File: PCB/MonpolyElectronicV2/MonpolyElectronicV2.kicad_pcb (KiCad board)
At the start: 2 copper layers, 0.7 x 0.5 mm, 92 parts, among them J1 Conn_01x14, J2 10155435-00011LF, J3 2171820001, J4 Conn_01x05, J5 Conn_01x04, J6 Conn_01x10, J7 Conn_01x05, Q1 NPN, Q2 NPN, Q3 AO3400A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

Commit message: finish placement of all components
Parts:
- added J10: Conn_01x01, Connector_PinHeader_2.54mm:PinHeader_1x01_P2.54mm_Vertical, F.Cu at (-47.0, 71.7)
- added J11: Conn_01x01, Connector_PinHeader_2.54mm:PinHeader_1x01_P2.54mm_Vertical, F.Cu at (-36.6, 86.0)
- added J12: Conn_01x01, Connector_PinHeader_2.54mm:PinHeader_1x01_P2.54mm_Vertical, F.Cu at (-20.2, 74.2)
- added J13: Conn_01x01, Connector_PinHeader_2.54mm:PinHeader_1x01_P2.54mm_Vertical, F.Cu at (-13.2, 73.0)
- added J14: Conn_01x01, Connector_PinHeader_2.54mm:PinHeader_1x01_P2.54mm_Vertical, F.Cu at (-16.7, 71.7)
- added J15: Conn_01x01, Connector_PinHeader_2.54mm:PinHeader_1x01_P2.54mm_Vertical, F.Cu at (-20.2, 70.5)
- added J16: Conn_01x01, Connector_PinHeader_2.54mm:PinHeader_1x01_P2.54mm_Vertical, F.Cu at (-26.5, 89.5)
- added J17: Conn_01x01, Connector_PinHeader_2.54mm:PinHeader_1x01_P2.54mm_Vertical, F.Cu at (-39.2, 89.5)
- added J18: Conn_01x01, Connector_PinHeader_2.54mm:PinHeader_1x01_P2.54mm_Vertical, F.Cu at (-29.1, 86.0)
- added J19: Conn_01x01, Connector_PinHeader_2.54mm:PinHeader_1x01_P2.54mm_Vertical, F.Cu at (-27.8, 93.0)
- added J8: Conn_01x01, Connector_PinHeader_2.54mm:PinHeader_1x01_P2.54mm_Vertical, F.Cu at (-20.2, 66.6)
- added J9: Conn_01x01, Connector_PinHeader_2.54mm:PinHeader_1x01_P2.54mm_Vertical, F.Cu at (-40.5, 86.0)
- added JP7: SolderJumper_2_Open, Jumper:SolderJumper-2_P1.3mm_Open_TrianglePad1.0x1.5mm, F.Cu at (176.4, 77.2)
- added R26: 10k, Resistor_SMD:R_0603_1608Metric, F.Cu at (-21.9, 80.5)
- C18: value 0.1uF -> 10uF
- J6: value Conn_01x10 -> Conn_01x01; footprint Connector_PinHeader_2.54mm:PinHeader_1x10_P2.54mm_Vertical -> Connector_PinHeader_2.54mm:PinHeader_1x01_P2.54mm_Vertical
- J7: value Conn_01x05 -> Conn_01x01; footprint Connector_PinHeader_2.54mm:PinHeader_1x05_P2.54mm_Vertical -> Connector_PinHeader_2.54mm:PinHeader_1x01_P2.54mm_Vertical
- R13: value 10k -> 100
- SW1, SW2, SW3: footprint Button_Switch_THT:SW_PUSH-12mm -> Extra:SW_TL1105BF160Q
- moved R14 146.3 mm to (-45.1, 67.2), turned to 180 degrees
- moved J5 142.7 mm to (129.8, 161.8), turned to -90 degrees
- moved C18 141.5 mm to (-44.2, 64.8), turned to 90 degrees
- moved JP4 136.3 mm to (182.8, 74.6), turned to 180 degrees
- moved JP5 133.9 mm to (182.8, 80.6), turned to 180 degrees
- moved R21 131.5 mm to (175.5, 70.6), turned to 90 degrees
- moved JP6 130.7 mm to (182.8, 87.4), turned to 180 degrees
- moved Q3 127.4 mm to (177.9, 81.5), turned to 90 degrees
- moved JP1 124.9 mm to (170.8, 74.6), turned to 180 degrees
- moved Q4 124.3 mm to (178.3, 89.1), turned to 90 degrees
- moved R23 122.6 mm to (177.9, 84.4)
- moved JP2 122.4 mm to (170.8, 80.6), turned to 180 degrees
- moved R22 120.4 mm to (174.5, 84.4)
- moved R25 119.9 mm to (178.3, 92.0), turned to 180 degrees
- moved JP3 119.2 mm to (170.8, 87.4), turned to 180 degrees
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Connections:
- C18 pad 1: GND -> +3.3V
- C18 pad 2: IO0 -> GND
- C19 pad 1: GND -> EN
- C19 pad 2: EN -> GND
- JP4 pad 2: Net-(JP1-A) -> Net-(JP4-B)
- R13 pad 1: IO0 -> Net-(JP1-A)
- R13 pad 2: +3.3V -> Net-(JP4-B)
- U1 pad 15: Net-(J7-Pin_3) -> Net-(J9-Pin_1)
- U1 pad 16: Net-(J6-Pin_7) -> Net-(J17-Pin_1)
- U1 pad 18: Net-(J7-Pin_5) -> Net-(J11-Pin_1)
- U1 pad 24: Net-(J6-Pin_8) -> Net-(J18-Pin_1)
- U1 pad 25: Net-(J6-Pin_9) -> Net-(J19-Pin_1)
- U1 pad 26: Net-(J6-Pin_6) -> Net-(J16-Pin_1)
- U1 pad 32: Net-(J6-Pin_2) -> Net-(J12-Pin_1)
- U1 pad 33: Net-(J6-Pin_3) -> Net-(J13-Pin_1)
- U1 pad 34: Net-(J6-Pin_4) -> Net-(J14-Pin_1)
- U1 pad 35: Net-(J6-Pin_5) -> Net-(J15-Pin_1)
- U1 pad 38: Net-(J7-Pin_2) -> Net-(J8-Pin_1)
- U1 pad 7: Net-(J7-Pin_4) -> Net-(J10-Pin_1)
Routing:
- net ESP32_D+: track 0.00 -> 6.09 mm
- net ESP32_D-: track 0.00 -> 6.04 mm
- net D-: track 2.62 -> 0.00 mm
- net D+: track 2.62 -> 0.00 mm

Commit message: finish placing components
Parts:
- BT1, TH1: moved to B.Cu
- J1: footprint Connector_PinHeader_2.54mm:PinHeader_1x14_P2.54mm_Vertical -> Extra:240X320 TFT 3.2 display
- moved C17 232.7 mm to (182.4, 102.3), turned to 0 degrees
- moved R5 232.0 mm to (171.2, 102.9), turned to -90 degrees
- moved C20 231.4 mm to (182.4, 103.8), turned to 0 degrees
- moved C18 230.3 mm to (182.4, 105.2), turned to 0 degrees
- moved R6 230.2 mm to (169.6, 102.9), turned to -90 degrees
- moved R14 228.2 mm to (180.0, 104.4), turned to 90 degrees
- moved J10 224.6 mm to (175.5, 102.5), turned to -90 degrees
- moved U1 216.4 mm to (177.8, 116.0), turned to -90 degrees
- moved R18 212.7 mm to (165.5, 102.8)
- moved R19 212.7 mm to (165.5, 104.4)
- moved J8 210.4 mm to (180.6, 129.2), turned to -90 degrees
- moved J7 209.7 mm to (181.8, 132.8), turned to -90 degrees
- moved J15 205.6 mm to (176.7, 129.2), turned to -90 degrees
- moved J9 203.1 mm to (161.2, 109.0), turned to -90 degrees
- moved J14 201.7 mm to (175.5, 132.8), turned to -90 degrees
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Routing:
- net D-: track 0.00 -> 30.2 mm, vias 0 -> 2
- net D+: track 0.00 -> 27.7 mm, vias 0 -> 2
- net ESP32_D-: track 6.04 -> 18.3 mm
- net ESP32_D+: track 6.09 -> 18.0 mm
- net /Logic/SCL: track 0.00 -> 10.5 mm, vias 0 -> 2
- net VUSB: track 0.00 -> 5.22 mm
- net Net-(U1-USB_D-): track 0.00 -> 5.14 mm
- net /Logic/SDA: track 0.00 -> 4.40 mm
- net Net-(U1-USB_D+): track 0.00 -> 2.86 mm
- net GND: track 0.00 -> 0.93 mm, vias 0 -> 1
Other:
- board size 0.7 x 0.5 mm -> 93.3 x 128.4 mm
- board text added: "NFC Module"

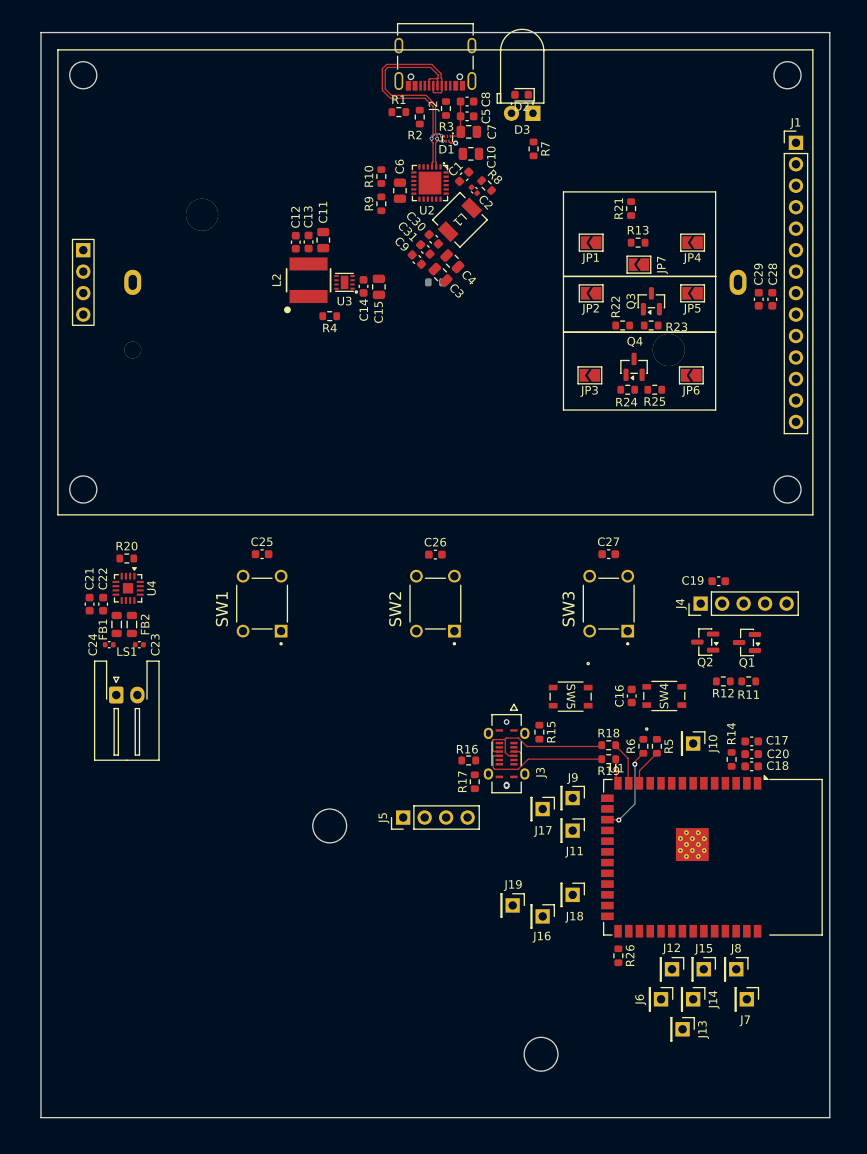
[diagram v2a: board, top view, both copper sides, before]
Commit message: start routing top part of the pcb
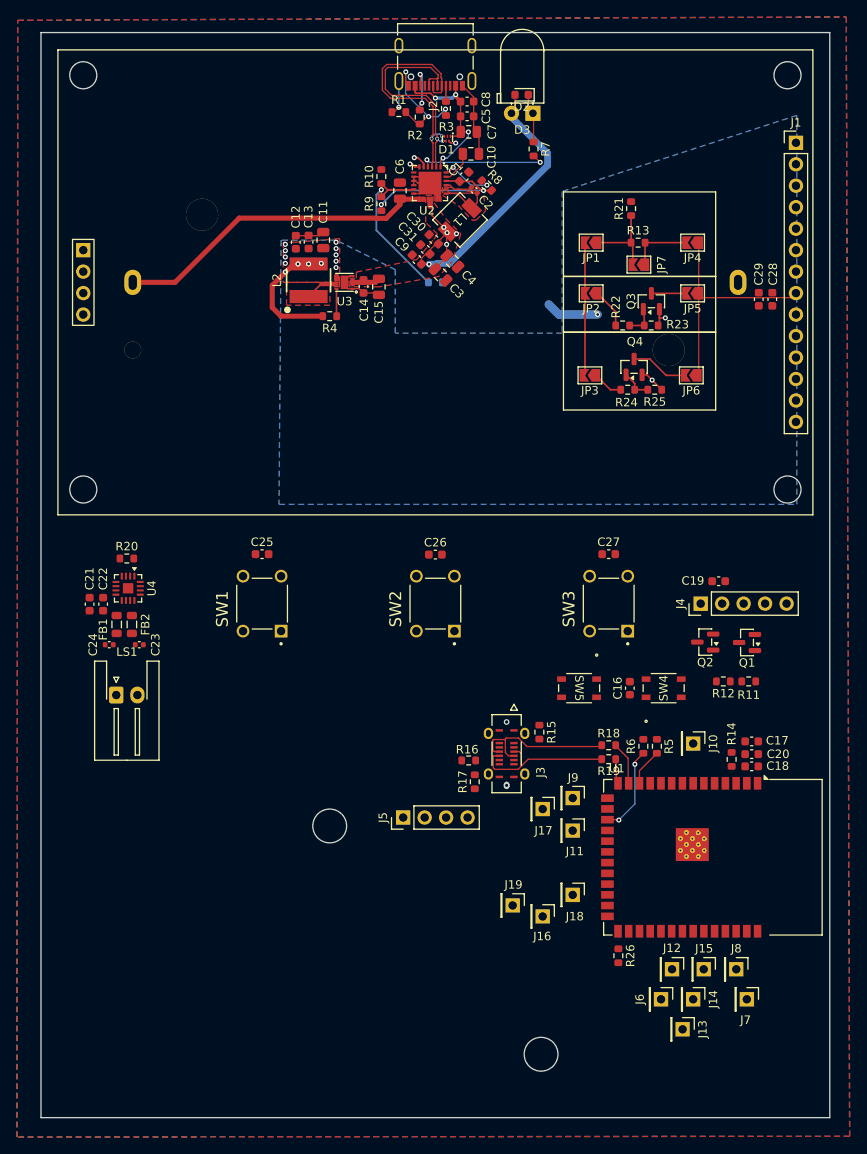
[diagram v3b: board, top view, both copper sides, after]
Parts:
- moved SW5 1.41 mm to (162.0, 96.0)
- moved C16 0.95 mm to (168.0, 96.0)
- moved SW4 0.93 mm to (172.0, 96.0)
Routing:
- net GND: track 0.93 -> 54.2 mm, vias 1 -> 6
- net SYS: track 0.00 -> 51.3 mm, vias 0 -> 5
- net BAT: track 0.00 -> 39.0 mm
- net TFT_LED: track 0.00 -> 27.7 mm
- net TS: track 0.00 -> 23.6 mm, vias 0 -> 1
- net REGN: track 0.00 -> 19.4 mm, vias 0 -> 2
- net +3.3V: track 0.00 -> 17.8 mm, vias 0 -> 14
- net Net-(JP1-B): track 0.00 -> 15.8 mm
- net Net-(U2-STAT): track 0.00 -> 15.5 mm, vias 0 -> 2
- net VUSB: track 5.22 -> 20.0 mm, vias 0 -> 4
- net Net-(JP1-A): track 0.00 -> 9.88 mm
- net Net-(C2-Pad2): track 0.00 -> 9.63 mm
- net Net-(JP4-B): track 0.00 -> 7.50 mm
- net Net-(JP6-B): track 0.00 -> 6.85 mm
- net DSEL: track 0.00 -> 6.79 mm, vias 0 -> 2
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- added copper zone on B.Cu, net +3.3V
- added copper zone on F.Cu, net +3.3V
- added copper zone on B.Cu, net GND
- added copper zone on F.Cu, net GND
- added copper zone on F.Cu, net Net-(C2-Pad2)
- added copper zone on F.Cu, net Net-(U3-SW)
- added copper zone on F.Cu, net SYS

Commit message: Finish routing PCB
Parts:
- removed J11, J17, J6, J9: Conn_01x01, Connector_PinHeader_2.54mm:PinHeader_1x01_P2.54mm_Vertical
- moved C27 41.0 mm to (124.5, 80.2)
- moved C25 41.0 mm to (165.4, 80.1)
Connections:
- U1 pad 15: Net-(J9-Pin_1) -> SW1
- U1 pad 16: Net-(J17-Pin_1) -> SW3
- U1 pad 18: Net-(J11-Pin_1) -> SW2
- U1 pad 31: Net-(J6-Pin_1) -> TFT_RESET
- U1 pad 8: TFT_RESET -> unconnected-(U1-IO15-Pad8)
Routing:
- net +3.3V: track 17.8 -> 240.1 mm, vias 14 -> 21
- net /Logic/SCL: track 12.3 -> 128.8 mm, vias 3 -> 6
- net /Logic/SDA: track 5.65 -> 122.1 mm, vias 1 -> 4
- net TFT_CS: track 0.00 -> 103.0 mm, vias 0 -> 2
- net Net-(JP1-B): track 15.8 -> 110.0 mm, vias 0 -> 2
- net TFT_RESET: track 0.00 -> 94.1 mm
- net TFT_DC: track 0.00 -> 85.9 mm
- net MOSI: track 0.00 -> 84.4 mm, vias 0 -> 1
- net DIN: track 0.00 -> 84.0 mm, vias 0 -> 2
- net SCK: track 0.00 -> 83.2 mm, vias 0 -> 3
- net MISO: track 0.00 -> 83.2 mm, vias 0 -> 1
- net BCLK: track 0.00 -> 81.9 mm
- net LRCLK: track 0.00 -> 79.7 mm
- net TFT_T_CS: track 0.00 -> 75.0 mm, vias 0 -> 1
- net GND: track 54.2 -> 121.9 mm, vias 6 -> 28
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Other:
- outline, holes or cut-outs redrawn
- board text added: "EN"
- board text added: "GND RTS DTR RX TX"
- board text added: "IO0"
